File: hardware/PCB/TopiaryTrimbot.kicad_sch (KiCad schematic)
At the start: 4 parts

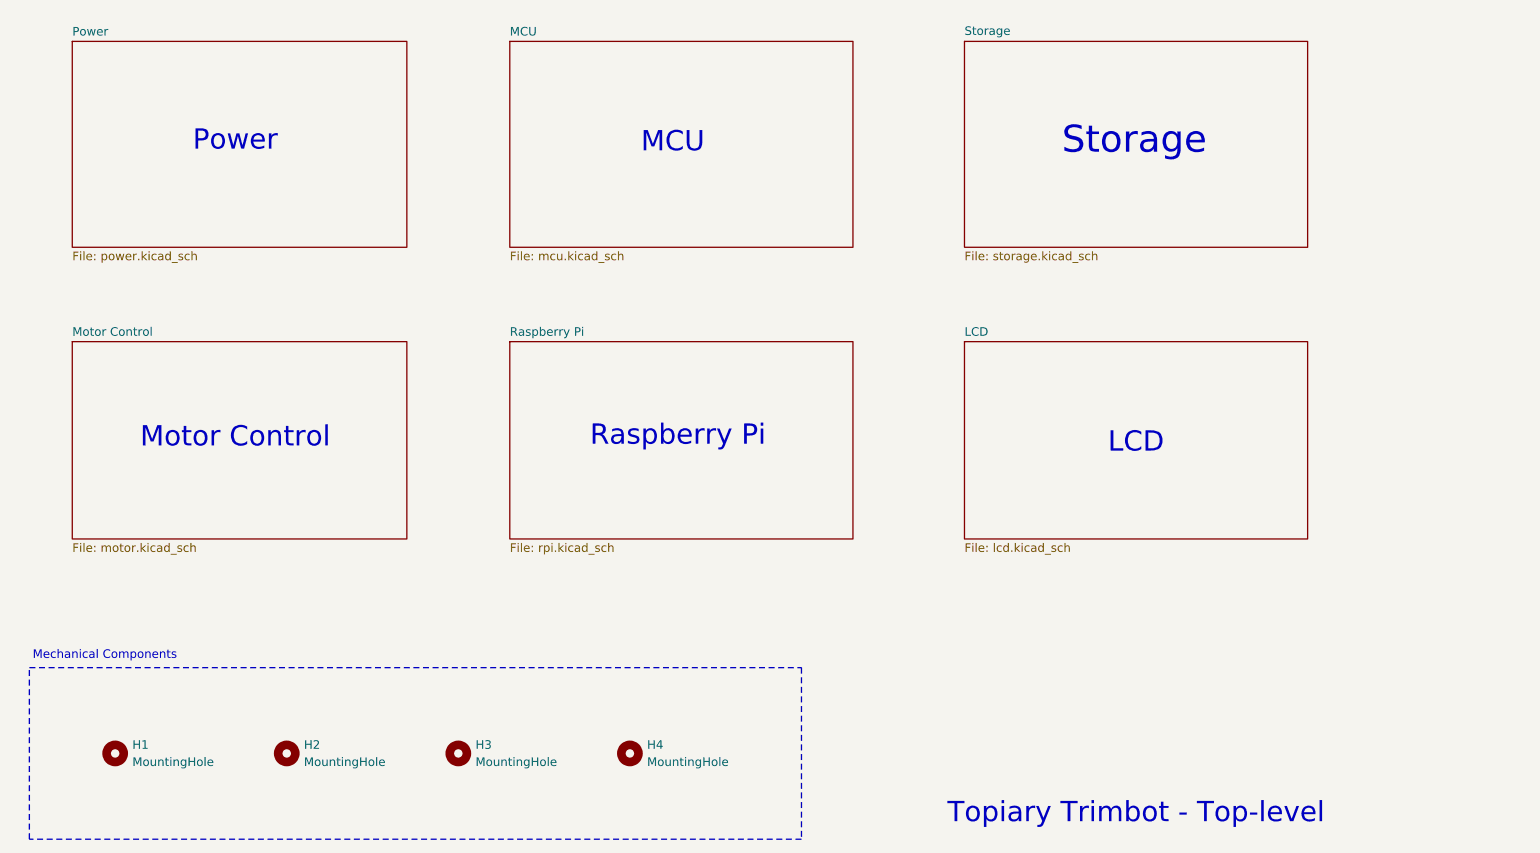
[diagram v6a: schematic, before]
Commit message: Add footprint for switch and wrap up footprint assignments for MCU
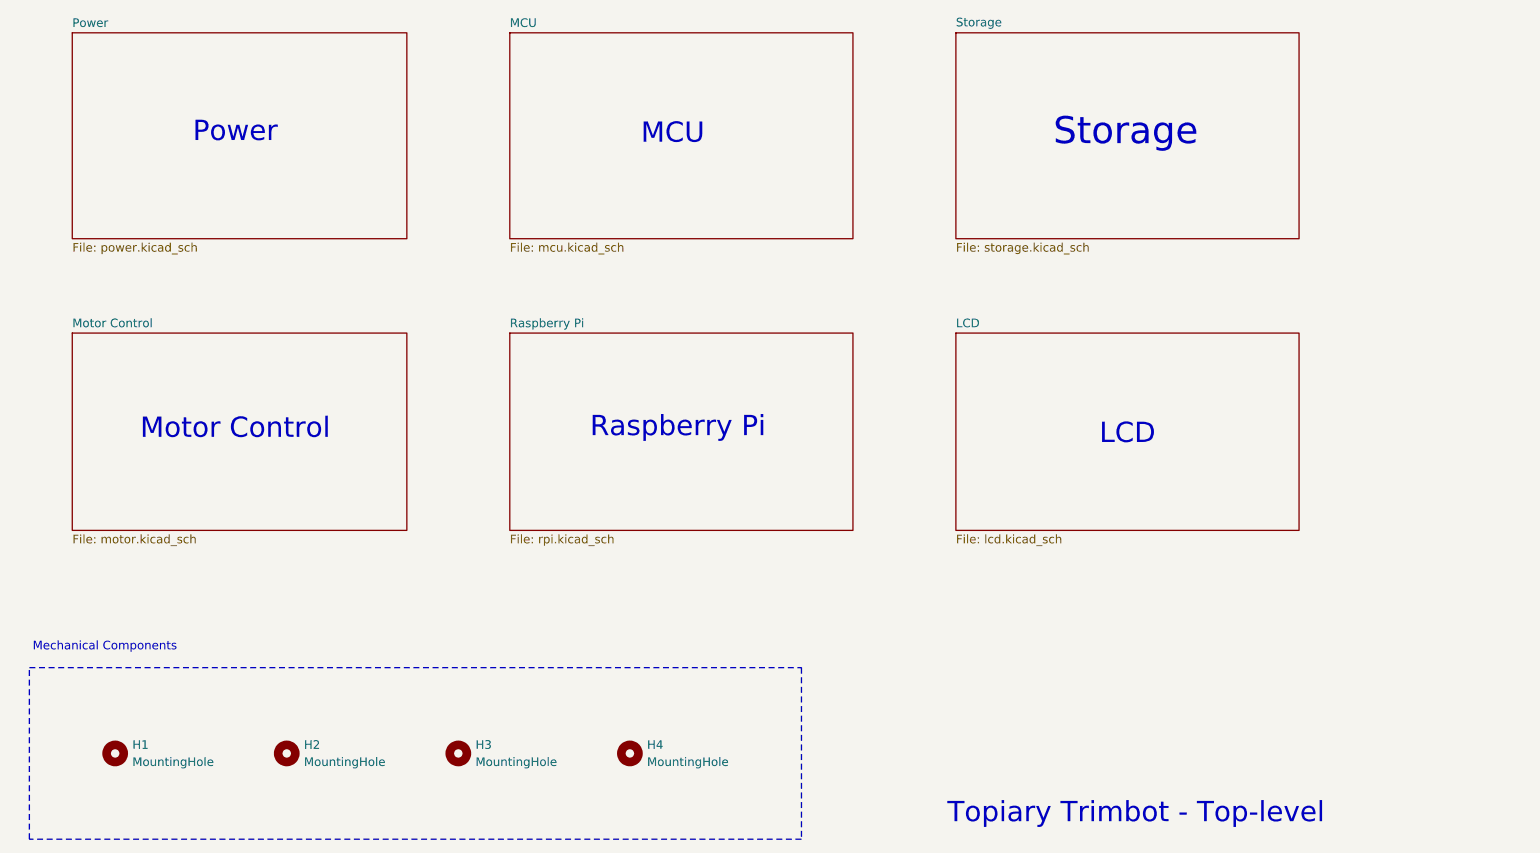
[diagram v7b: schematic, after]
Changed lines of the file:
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@@
 	(text "Raspberry Pi"
 		(exclude_from_sim no)
-		(at 146.812 118.11 0)
+		(at 146.812 116.84 0)
 		(effects
 			(font
@@
 	(text "Mechanical Components"
 		(exclude_from_sim no)
-		(at 61.976 150.622 0)
+		(at 61.976 149.352 0)
 		(effects
 			(font
@@
 	(text "Power"
 		(exclude_from_sim no)
-		(at 81.28 74.422 0)
+		(at 81.28 73.152 0)
 		(effects
 			(font
@@
 	(text "Storage"
 		(exclude_from_sim no)
-		(at 214.376 74.422 0)
+		(at 213.106 73.152 0)
 		(effects
 			(font
@@
 	(text "Motor Control"
 		(exclude_from_sim no)
-		(at 81.28 118.364 0)
+		(at 81.28 117.094 0)
 		(effects
 			(font
@@
 	(text "MCU"
 		(exclude_from_sim no)
-		(at 146.05 74.676 0)
+		(at 146.05 73.406 0)
 		(effects
 			(font
@@
 	(text "LCD"
 		(exclude_from_sim no)
-		(at 214.63 119.126 0)
+		(at 213.36 117.856 0)
 		(effects
 			(font
@@
 	)
 	(sheet
-		(at 189.23 59.69)
+		(at 187.96 58.42)
 		(size 50.8 30.48)
 		(exclude_from_sim no)
@@
 		)
 		(property "Sheetname" "Storage"
-			(at 189.23 57.404 0)
+			(at 187.96 56.134 0)
 			(effects
 				(font
@@
 		)
 		(property "Sheetfile" "storage.kicad_sch"
-			(at 189.23 90.7546 0)
+			(at 187.96 89.4846 0)
 			(effects
 				(font
@@
 		)
 		(property "Field2" ""
-			(at 189.23 59.69 0)
+			(at 187.96 58.42 0)
 			(effects
 				(font
@@
 	)
 	(sheet
-		(at 57.15 104.14)
+		(at 57.15 102.87)
 		(size 49.53 29.21)
 		(exclude_from_sim no)
@@
 		)
 		(property "Sheetname" "Motor Control"
-			(at 57.15 103.4284 0)
+			(at 57.15 102.1584 0)
 			(effects
 				(font
@@
 		)
 		(property "Sheetfile" "motor.kicad_sch"
-			(at 57.15 133.9346 0)
+			(at 57.15 132.6646 0)
 			(effects
 				(font
@@
 	)
 	(sheet
-		(at 121.92 59.69)
+		(at 121.92 58.42)
 		(size 50.8 30.48)
 		(exclude_from_sim no)
@@
 		)
 		(property "Sheetname" "MCU"
-			(at 121.92 58.9784 0)
+			(at 121.92 57.7084 0)
 			(effects
 				(font
@@
 		)
 		(property "Sheetfile" "mcu.kicad_sch"
-			(at 121.92 90.7546 0)
+			(at 121.92 89.4846 0)
 			(effects
 				(font
@@
 		)
 		(property "Field2" ""
-			(at 121.92 59.69 0)
+			(at 121.92 58.42 0)
 			(effects
 				(font
@@
 	)
 	(sheet
-		(at 57.15 59.69)
+		(at 57.15 58.42)
 		(size 49.53 30.48)
 		(exclude_from_sim no)
@@
 		)
 		(property "Sheetname" "Power"
-			(at 57.15 58.9784 0)
+			(at 57.15 57.7084 0)
 			(effects
 				(font
@@
 		)
 		(property "Sheetfile" "power.kicad_sch"
-			(at 57.15 90.7546 0)
+			(at 57.15 89.4846 0)
 			(effects
 				(font
@@
 		)
 		(property "Field2" ""
-			(at 57.15 59.69 0)
+			(at 57.15 58.42 0)
 			(effects
 				(font
@@
 	)
 	(sheet
-		(at 121.92 104.14)
+		(at 121.92 102.87)
 		(size 50.8 29.21)
 		(exclude_from_sim no)
@@
 		)
 		(property "Sheetname" "Raspberry Pi"
-			(at 121.92 103.4284 0)
+			(at 121.92 102.1584 0)
 			(effects
 				(font
@@
 		)
 		(property "Sheetfile" "rpi.kicad_sch"
-			(at 121.92 133.9346 0)
+			(at 121.92 132.6646 0)
 			(effects
 				(font
@@
 		)
 		(property "Field2" ""
-			(at 121.92 104.14 0)
+			(at 121.92 102.87 0)
 			(effects
 				(font
@@
 	)
 	(sheet
-		(at 189.23 104.14)
+		(at 187.96 102.87)
 		(size 50.8 29.21)
 		(exclude_from_sim no)
@@
 		)
 		(property "Sheetname" "LCD"
-			(at 189.23 103.4284 0)
+			(at 187.96 102.1584 0)
 			(effects
 				(font
@@
 		)
 		(property "Sheetfile" "lcd.kicad_sch"
-			(at 189.23 133.9346 0)
-			(effects
-				(font
+			(at 187.96 132.6646 0)
+			(effects
+				(font
